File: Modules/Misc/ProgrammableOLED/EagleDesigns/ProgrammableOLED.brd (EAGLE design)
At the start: 100 x 80 mm, 14 parts, among them U2 ATMEGA328P_TQFP

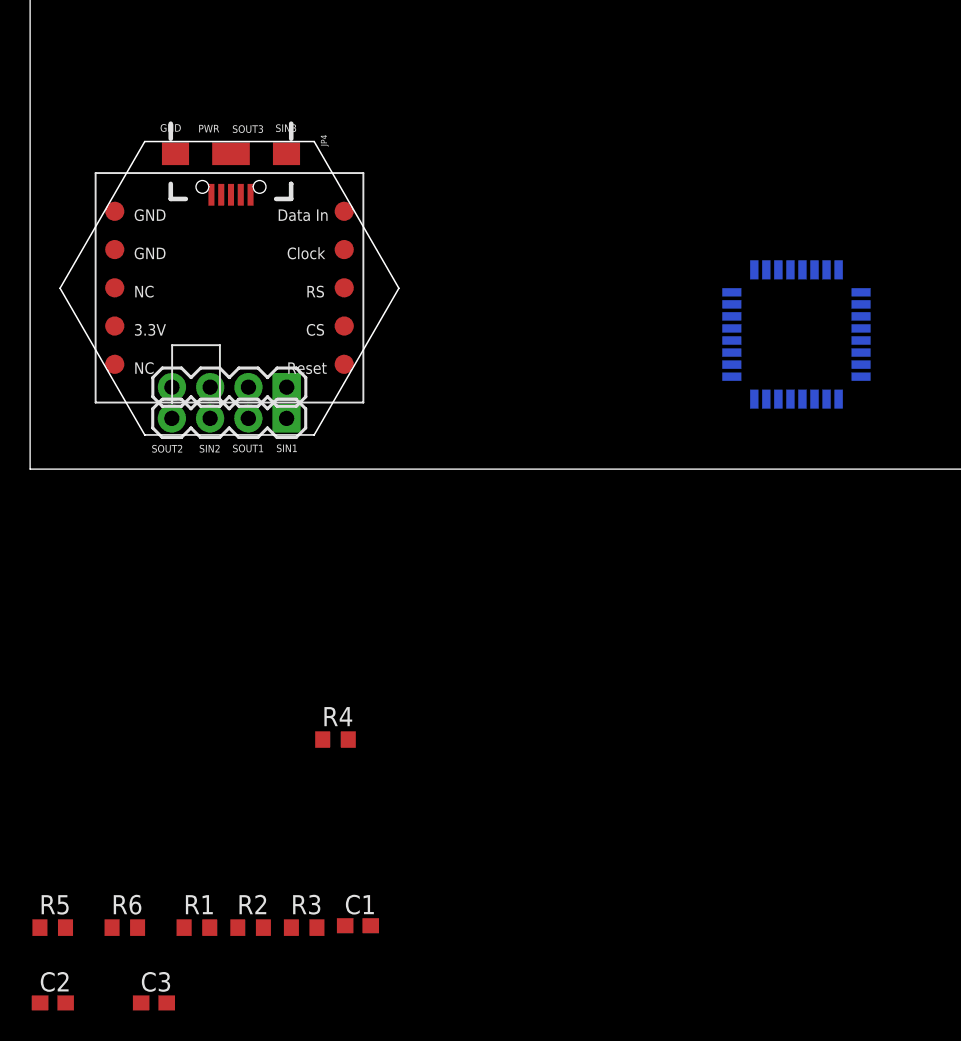
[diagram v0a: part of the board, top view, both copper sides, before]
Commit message: deleted the other incomplete programmable module
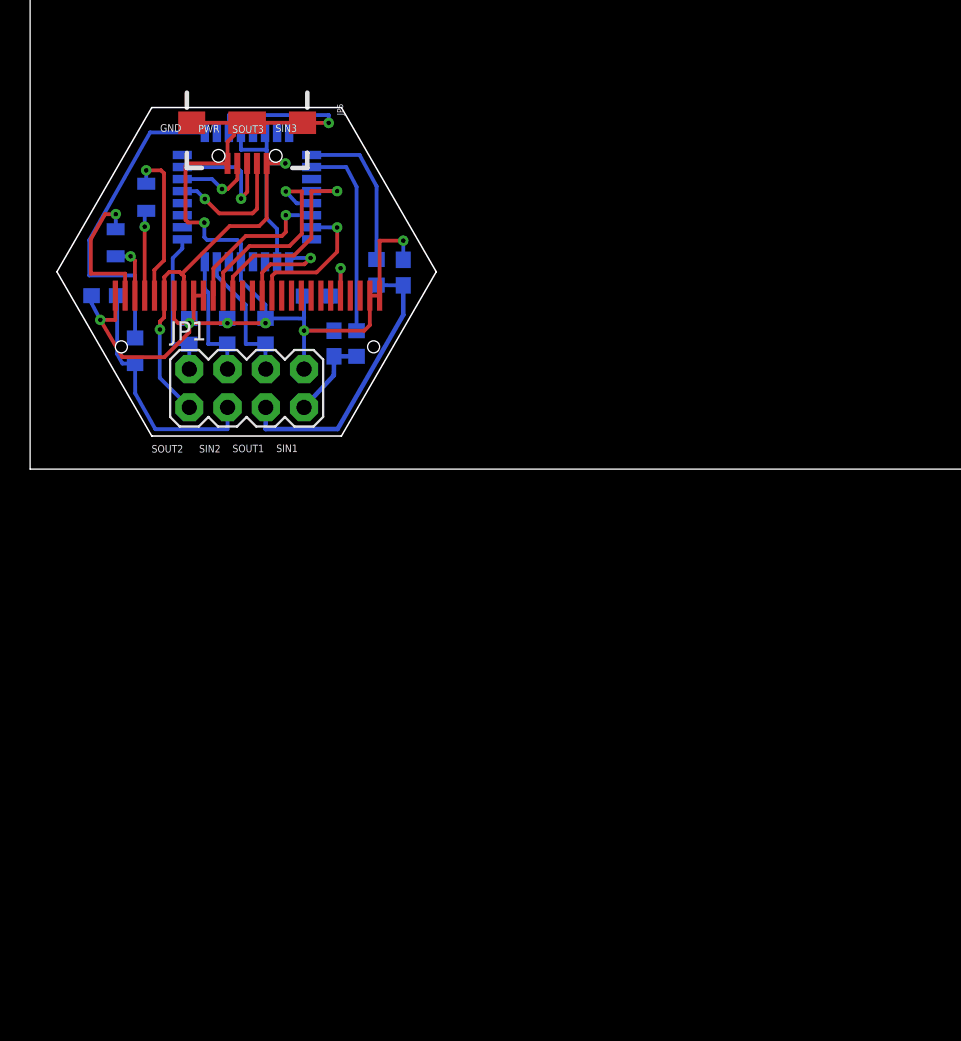
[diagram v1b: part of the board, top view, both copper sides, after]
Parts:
- removed JP2: (no value), SparkFun-Connectors:1X04
- removed JP4: (no value), SparkFun-Connectors:USB-B-MICRO-SMD_V03
- removed U$1: OLED, MakerWear:OLED
- added C4, C5: 1uF X5R, SparkFun-Passives:0805
- added JP5: (no value), SparkFun-Connectors:USB-AB-MICRO-SMD_V03
- added OLED1: OLED0.66, microView-temp:OLED-0.66-64X48
- added R7: 390k, SparkFun-Passives:0603-RES
- JP1: device SparkFun-Connectors:1X04 -> SparkFun-Connectors:2X4
- moved R5 48.5 mm to (23.0, 13.1), flipped to the bottom, turned to 90 degrees
- moved C2 47.6 mm to (20.2, 8.34), flipped to the bottom, turned to 90 degrees
- moved C3 47.1 mm to (4.93, 11.5), flipped to the bottom
- moved C1 43.5 mm to (24.8, 13.1), flipped to the bottom, turned to 90 degrees
- moved R6 41.7 mm to (21.7, 8.34), flipped to the bottom, turned to 90 degrees
- moved R3 39.7 mm to (15.6, 9.16), flipped to the bottom, turned to 270 degrees
- moved R2 39.6 mm to (13.1, 9.16), flipped to the bottom, turned to 270 degrees
- moved R1 39.6 mm to (10.6, 9.15), flipped to the bottom, turned to 270 degrees
- moved U2 37.6 mm to (14.4, 18.1), turned to 270 degrees
- moved R4 29.0 mm to (6.97, 7.86), flipped to the bottom, turned to 90 degrees
- moved JP1 3.32 mm to (14.4, 5.37), turned to 0 degrees
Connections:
- removed net OLED_CLK: U$1.CLOCK
- removed net OLED_CS: U$1.CS
- removed net OLED_DATA: U$1.DATA_IN
- removed net OLED_RESET: U$1.RESET
- removed net OLED_RS: U$1.RS
- new net C1N: C4.2, OLED1.5
- new net C1P: C4.1, OLED1.4
- new net C2N: C5.2, OLED1.3
- new net C2P: C5.1, OLED1.2
- new net IREF: OLED1.24, R7.2
- new net OLED-CS: OLED1.11, U2.14
- new net OLED-D/C: OLED1.13, U2.12
- new net OLED-MOSI: OLED1.17, U2.15
- new net OLED-RST: OLED1.12, U2.13
- new net OLED-SCK: OLED1.16, U2.17
- net GND: now also JP1.8, JP5.GND1, JP5.SHIELD1, JP5.SHIELD2, JP5.SHIELD3, OLED1.1, OLED1.10, OLED1.27, OLED1.28, OLED1.7, OLED1.9, R7.1; no longer JP2.1, JP4.GND1, JP4.SHIELD1, JP4.SHIELD2, JP4.SHIELD3, U$1.GND1, U$1.GND2
- net OUT1: now also U2.1; no longer U2.9
- net OUT2: now also U2.9; no longer U2.13
- net OUT3: now also U2.10; no longer U2.14
- net RESET: now also JP5.D-1; no longer JP4.ID1
- net RX: now also JP5.ID1; no longer JP4.D-1
- net SIN1: now also JP1.6; no longer JP2.2
- net SIN2: now also JP1.4; no longer JP2.3
- net SIN3: now also JP1.2; no longer JP2.4
- net SOUT2: now also JP1.5; no longer JP1.2
- net SOUT3: now also JP1.7; no longer JP1.1
- net TX: now also JP5.D+1; no longer JP4.D+1
- net VCC: now also JP1.1, JP5.VBUS1, OLED1.6, OLED1.8; no longer JP1.4, JP4.VBUS1, U$1.3.3V
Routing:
- net GND: track 0.00 -> 86.2 mm, vias 0 -> 8
- net VCC: track 0.00 -> 37.7 mm, vias 0 -> 2
- net OUT1: track 0.00 -> 21.4 mm
- net SOUT2: track 0.00 -> 18.7 mm
- net SOUT1: track 0.00 -> 16.4 mm
- net OLED-D/C: track 0.00 -> 14.1 mm, vias 0 -> 1
- net OLED-RST: track 0.00 -> 13.8 mm, vias 0 -> 1
- net OUT3: track 0.00 -> 13.3 mm
- net C1N: track 0.00 -> 10.5 mm, vias 0 -> 1
- net OLED-CS: track 0.00 -> 10.5 mm, vias 0 -> 1
- net OUT2: track 0.00 -> 10.4 mm
- net SIN3: track 0.00 -> 9.99 mm
- net C2P: track 0.00 -> 9.66 mm, vias 0 -> 1
- net OLED-MOSI: track 0.00 -> 9.62 mm, vias 0 -> 1
- net SIN1: track 0.00 -> 9.24 mm
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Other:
- outline, holes or cut-outs redrawn

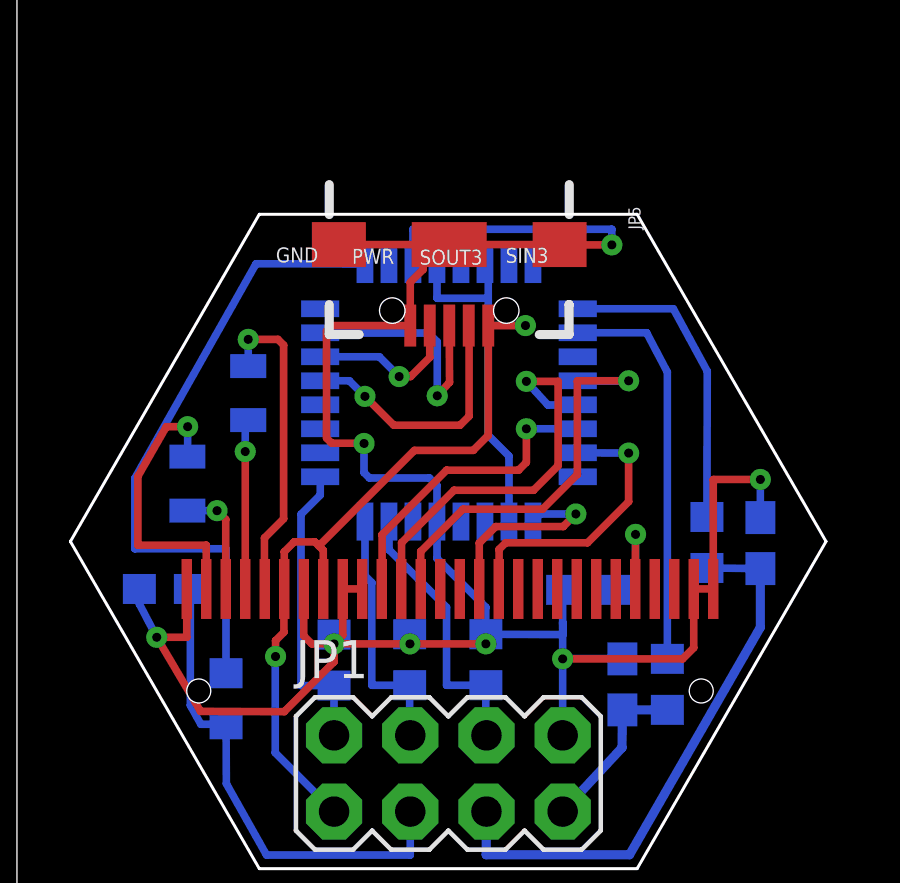
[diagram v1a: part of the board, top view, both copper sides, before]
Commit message: moved MicroUSB more into the hexagon, removed holes for MicroUSB & OLED
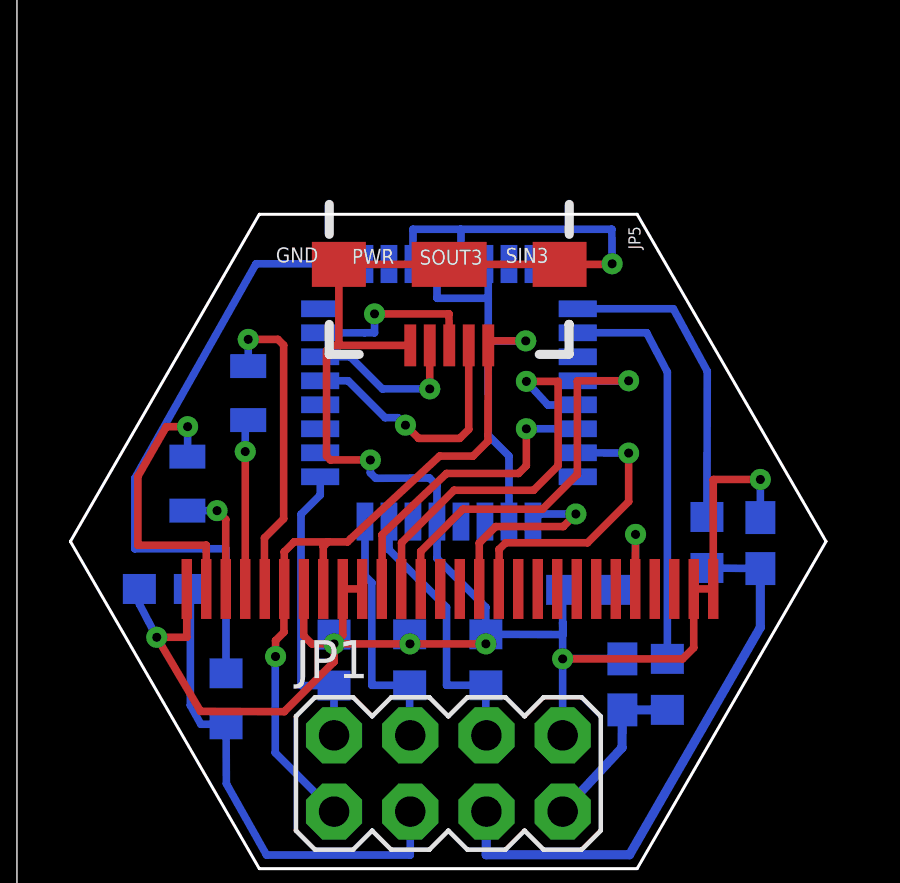
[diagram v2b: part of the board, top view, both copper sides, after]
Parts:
- moved JP5 0.66 mm to (14.4, 22.3)
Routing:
- net TX: track 8.37 -> 6.01 mm

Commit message: another round of minor fixes
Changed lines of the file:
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@@
 <layer number="21" name="tPlace" color="7" fill="1" visible="no" active="yes"/>
 <layer number="22" name="bPlace" color="7" fill="1" visible="no" active="yes"/>
-<layer number="23" name="tOrigins" color="15" fill="1" visible="yes" active="yes"/>
-<layer number="24" name="bOrigins" color="15" fill="1" visible="yes" active="yes"/>
+<layer number="23" name="tOrigins" color="15" fill="1" visible="no" active="yes"/>
+<layer number="24" name="bOrigins" color="15" fill="1" visible="no" active="yes"/>
 <layer number="25" name="tNames" color="7" fill="1" visible="no" active="yes"/>
 <layer number="26" name="bNames" color="7" fill="1" visible="no" active="yes"/>
@@
 <layer number="112" name="tSilk" color="7" fill="1" visible="no" active="yes"/>
 <layer number="113" name="IDFDebug" color="4" fill="1" visible="no" active="yes"/>
-<layer number="114" name="Badge_Outline" color="7" fill="1" visible="yes" active="yes"/>
-<layer number="115" name="ReferenceISLANDS" color="7" fill="1" visible="yes" active="yes"/>
+<layer number="114" name="Badge_Outline" color="7" fill="1" visible="no" active="yes"/>
+<layer number="115" name="ReferenceISLANDS" color="7" fill="1" visible="no" active="yes"/>
 <layer number="116" name="Patch_BOT" color="9" fill="4" visible="no" active="yes"/>
-<layer number="118" name="Rect_Pads" color="7" fill="1" visible="yes" active="yes"/>
+<layer number="118" name="Rect_Pads" color="7" fill="1" visible="no" active="yes"/>
 <layer number="121" name="_tsilk" color="7" fill="1" visible="no" active="yes"/>
 <layer number="122" name="_bsilk" color="7" fill="1" visible="no" active="yes"/>
@@
 <layer number="127" name="_tValues" color="7" fill="1" visible="no" active="yes"/>
 <layer number="128" name="_bValues" color="7" fill="1" visible="no" active="yes"/>
-<layer number="129" name="Mask" color="7" fill="1" visible="yes" active="yes"/>
+<layer number="129" name="Mask" color="7" fill="1" visible="no" active="yes"/>
 <layer number="131" name="tAdjust" color="7" fill="1" visible="no" active="yes"/>
 <layer number="132" name="bAdjust" color="7" fill="1" visible="no" active="yes"/>
@@
 <wire x1="23.22" y1="15.17" x2="23.21" y2="15.16" width="0.254" layer="1"/>
 <wire x1="23.21" y1="15.16" x2="23.21" y2="11.52" width="0.254" layer="1"/>
-<wire x1="8.91" y1="7.43" x2="6.12" y2="7.44" width="0.254" layer="1"/>
-<wire x1="6.12" y1="7.44" x2="4.66" y2="9.91" width="0.254" layer="1"/>
+<wire x1="8.91" y1="7.43" x2="6.05" y2="7.43" width="0.254" layer="1"/>
+<wire x1="6.05" y1="7.43" x2="4.66" y2="9.91" width="0.254" layer="1"/>
 <via x="4.66" y="9.91" extent="1-16" drill="0.3" diameter="0.254"/>
 <wire x1="4.08" y1="11.52" x2="4.08" y2="11.02" width="0.254" layer="16"/>
@@
 <contactref element="JP5" pad="VBUS1"/>
 <wire x1="16.4" y1="13.7674" x2="16.42" y2="13.7874" width="0.254" layer="16"/>
-<wire x1="15.6" y1="22.3526" x2="15.69" y2="22.2626" width="0.254" layer="16"/>
 <wire x1="10.57" y1="4.1" x2="8.61" y2="6.06" width="0.254" layer="16"/>
 <wire x1="8.61" y1="6.06" x2="8.61" y2="9.26" width="0.254" layer="16"/>
@@
 <wire x1="15.2" y1="15.95" x2="15.7" y2="16.45" width="0.254" layer="1"/>
 <wire x1="15.7" y1="16.45" x2="15.71" y2="19.64" width="0.254" layer="1"/>
-<wire x1="15.71" y1="19.79" x2="15.71" y2="19.64" width="0.254" layer="1"/>
 <wire x1="16.4" y1="13.7674" x2="16.4" y2="15.95" width="0.254" layer="16"/>
-<wire x1="16.4" y1="15.95" x2="15.71" y2="16.64" width="0.254" layer="16"/>
-<wire x1="15.71" y1="21.18" x2="15.71" y2="22.2426" width="0.254" layer="16"/>
-<wire x1="15.71" y1="22.2426" x2="15.6" y2="22.3526" width="0.254" layer="16"/>
-<wire x1="14" y1="22.3526" x2="14" y2="21.22" width="0.254" layer="16"/>
-<wire x1="14" y1="21.22" x2="14.01" y2="21.21" width="0.254" layer="16"/>
-<wire x1="14.01" y1="21.21" x2="15.68" y2="21.21" width="0.254" layer="16"/>
-<wire x1="15.68" y1="21.21" x2="15.71" y2="21.18" width="0.254" layer="16"/>
-<wire x1="15.71" y1="21.18" x2="15.71" y2="19.79" width="0.254" layer="16"/>
-<wire x1="15.71" y1="19.79" x2="16.96" y2="19.79" width="0.254" layer="16"/>
-<via x="16.96" y="19.79" extent="1-16" drill="0.3"/>
-<wire x1="16.96" y1="19.79" x2="15.71" y2="19.79" width="0.254" layer="1"/>
-<wire x1="15.71" y1="16.64" x2="15.71" y2="19.79" width="0.254" layer="16"/>
 <wire x1="9.24" y1="13.09" x2="10.37" y2="13.09" width="0.254" layer="1"/>
 <wire x1="10.37" y1="13.09" x2="11.02" y2="13.09" width="0.254" layer="1"/>
 <wire x1="11.02" y1="13.09" x2="11.125" y2="13.195" width="0.254" layer="1"/>
 <wire x1="10.21" y1="12.93" x2="10.37" y2="13.09" width="0.254" layer="1"/>
+<wire x1="15.6" y1="22.3526" x2="15.6" y2="20.77" width="0.254" layer="16"/>
+<wire x1="15.6" y1="20.77" x2="15.6" y2="20.14" width="0.254" layer="16"/>
+<wire x1="15.6" y1="16.75" x2="16.4" y2="15.95" width="0.254" layer="16"/>
+<wire x1="14" y1="22.3526" x2="14" y2="21" width="0.254" layer="16"/>
+<wire x1="14" y1="21" x2="14.22" y2="20.78" width="0.254" layer="16"/>
+<wire x1="14.22" y1="20.78" x2="15.59" y2="20.78" width="0.254" layer="16"/>
+<wire x1="15.59" y1="20.78" x2="15.6" y2="20.77" width="0.254" layer="16"/>
+<wire x1="15.6" y1="16.75" x2="15.6" y2="20.14" width="0.254" layer="16"/>
+<wire x1="15.6" y1="20.14" x2="16.83" y2="20.14" width="0.254" layer="16"/>
+<wire x1="16.83" y1="20.14" x2="16.84" y2="20.13" width="0.254" layer="16"/>
+<via x="16.84" y="20.13" extent="1-16" drill="0.3"/>
+<wire x1="16.84" y1="20.13" x2="15.78" y2="20.13" width="0.254" layer="1"/>
+<wire x1="15.78" y1="20.13" x2="15.75" y2="20.16" width="0.254" layer="1"/>
+<wire x1="15.75" y1="20.16" x2="15.75" y2="19.68" width="0.254" layer="1"/>
+<wire x1="15.75" y1="19.68" x2="15.71" y2="19.64" width="0.254" layer="1"/>
 </signal>
 <signal name="RESET">
